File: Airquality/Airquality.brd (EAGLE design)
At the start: 70 x 70 mm, 68 parts, among them IC1 SCD41-D-R2, U1 SGP41-D-R4, U3 BMP581, U4 AP22802AW5-7K-3.3V

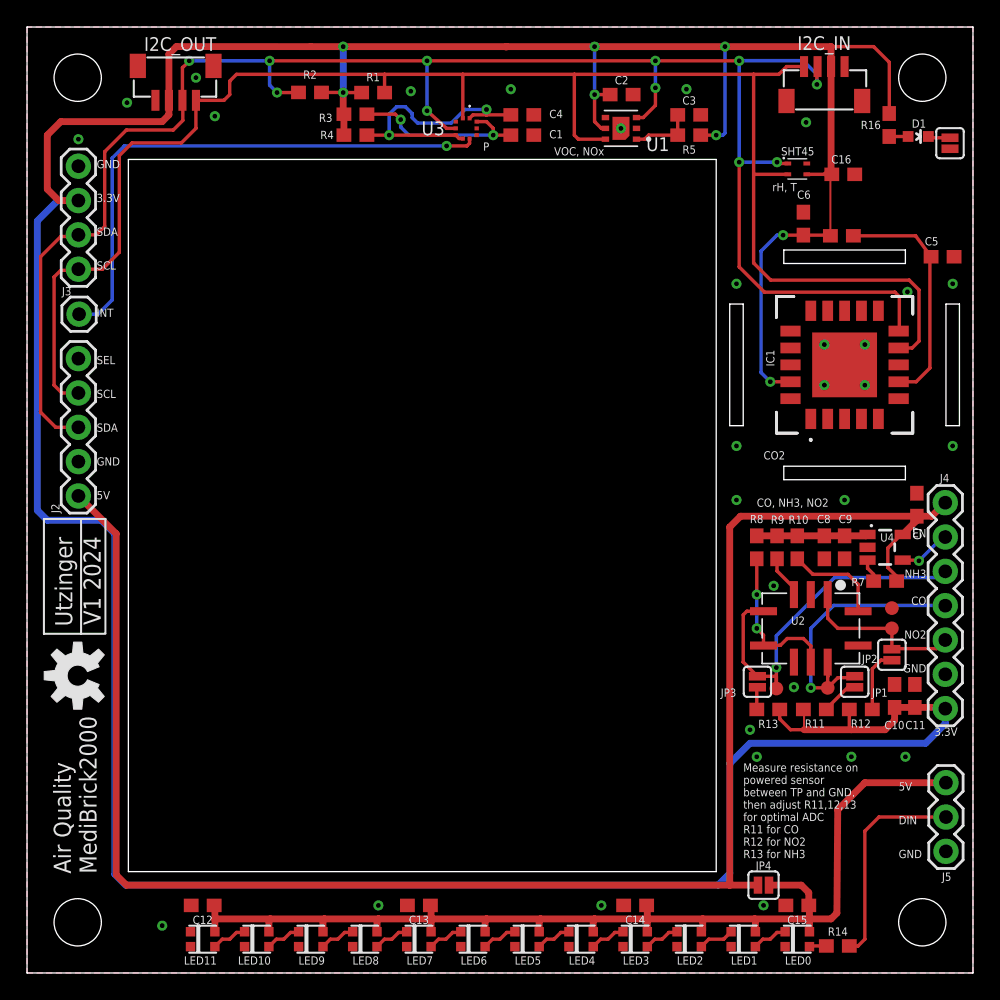
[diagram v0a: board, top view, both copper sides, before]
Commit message: Air Quality at 3.3V with 5V boost for PM sensor
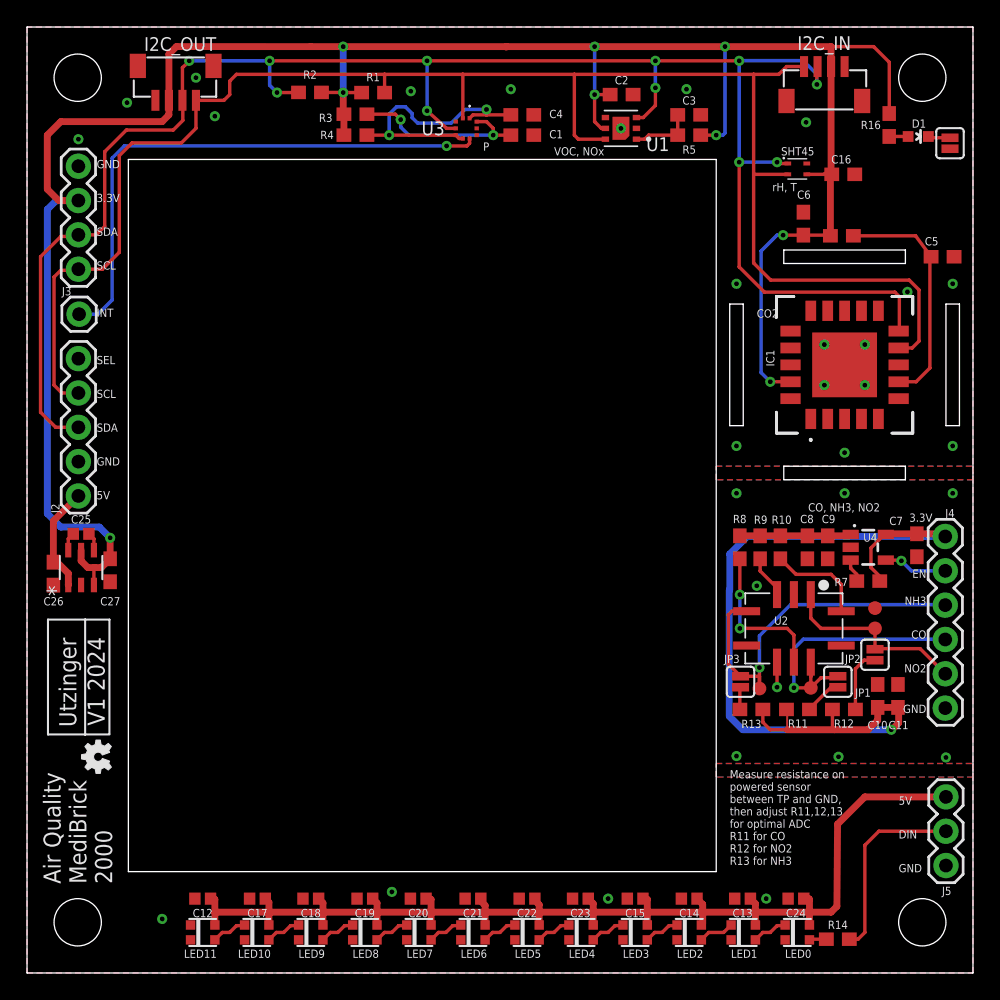
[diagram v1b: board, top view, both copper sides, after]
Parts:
- removed JP4: JUMPER-SMT_2_NO_SILK, SparkFun-Jumpers:SMT-JUMPER_2_NO_SILK
- added C17, C18, C19, C20, C21, C22, C23, C24: 0.1uF, SparkFun-Capacitors:0402
- added C25: 1.0uF, SparkFun-Capacitors:0402
- added C26, C27: 10uF, SparkFun-Capacitors:0603
- added U5: AP3602AKTR-G1, AP3602A:SOT-23-6_DIO
- C12, C13, C14, C15: value 10uF -> 0.1uF; device SparkFun-Capacitors:0603 -> SparkFun-Capacitors:0402
- J4: device SparkFun-Connectors:1X07 -> SparkFun-Connectors:1X06
- R10: value 130 -> 61
- R3: value 10 -> 0
- R4: value 10 -> 4.7
- R8: value 820 -> 29
- R9: value 27 -> 38
- U$2: device SparkFun-Aesthetics:OSHW-LOGO-M -> SparkFun-Aesthetics:OSHW-LOGO-MINI
- moved C13 24.0 mm to (53.0, 5.50)
- moved C15 12.0 mm to (45.0, 5.50)
- moved U$2 6.18 mm to (5.25, 16.0)
- moved C14 4.03 mm to (49.0, 5.50)
- moved C7 3.00 mm to (65.8, 31.6), turned to 270 degrees
- moved J4 2.50 mm to (68.0, 32.3)
- moved C10 1.25 mm to (63.0, 20.5)
- moved C11 1.25 mm to (64.5, 20.5)
- moved C8 1.25 mm to (57.8, 31.5)
- moved C9 1.25 mm to (59.2, 31.5)
- moved CO 1.25 mm to (58.0, 21.1)
- moved GND 1.25 mm to (62.8, 27.0)
- moved JP1 1.25 mm to (60.0, 21.6)
- moved JP2 1.25 mm to (62.8, 23.6)
- moved JP3 1.25 mm to (52.8, 21.6)
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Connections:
- removed net 5V: C12.1, C13.1, C14.1, C15.1, C7.1, J2.1, J4.1, J5.3, JP4.1, JP4.2, LED0.4, LED1.4, LED10.4, LED11.4, LED2.4, LED3.4, LED4.4, LED5.4, LED6.4, LED7.4, LED8.4, LED9.4, R7.1, U4.5
- new net N$15: C25.1, U5.6
- new net N$30: C25.2, U5.4
- new net N$31: C12.1, C13.1, C14.1, C15.1, C17.1, C18.1, C19.1, C20.1, C21.1, C22.1, C23.1, C24.1, J5.3, LED0.4, LED1.4, LED10.4, LED11.4, LED2.4, LED3.4, LED4.4, LED5.4, LED6.4, LED7.4, LED8.4, LED9.4
- new net VOUT: C26.1, J2.1, U5.1
- net 3.3V: now also C27.1, C7.1, J4.1, R7.1, U4.5, U5.3, U5.5; no longer J4.7
- net GND: now also C17.2, C18.2, C19.2, C20.2, C21.2, C22.2, C23.2, C24.2, C26.2, C27.2, U2.E, U5.2
- net N$13: no longer U2.E
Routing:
- net 5V: track 209.7 -> 0.00 mm
- net N$31: track 0.00 -> 87.9 mm
- net 3.3V: track 285.6 -> 242.3 mm, vias 8 -> 10
- net VOUT: track 0.00 -> 7.98 mm
- net GND: track 0.00 -> 1.85 mm, vias 30 -> 31
- net NO2: track 12.6 -> 14.3 mm
- net N$22: track 15.8 -> 14.2 mm
- net N$30: track 0.00 -> 1.36 mm
- net N$15: track 0.00 -> 1.36 mm
- net N$9: track 4.10 -> 4.93 mm
- net CO: track 20.6 -> 19.9 mm
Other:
- board text added: "Air Quality MediBrick 2000"
- board text removed: "Air Quality MediBrick2000"

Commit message: BOM
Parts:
- added FLG: TEST-POINT3X4, SparkFun-Connectors:PAD.03X.04
- added R15: 10k, SparkFun-Resistors:0603
- moved GND 3.16 mm to (65.8, 26.0)
- moved R7 1.00 mm to (62.2, 28.0), turned to 90 degrees
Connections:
- removed net N$9: J4.2, U4.4
- new net N$32: J4.2, R15.2, U4.4
- net 3.3V: now also R15.1
- net N$3: now also FLG.P$1
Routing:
- net N$32: track 0.00 -> 6.72 mm, vias 0 -> 1
- net N$9: track 4.93 -> 0.00 mm, vias 1 -> 0
- net 3.3V: track 242.3 -> 246.2 mm
- net N$3: track 1.74 -> 2.59 mm
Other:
- outline, holes or cut-outs redrawn

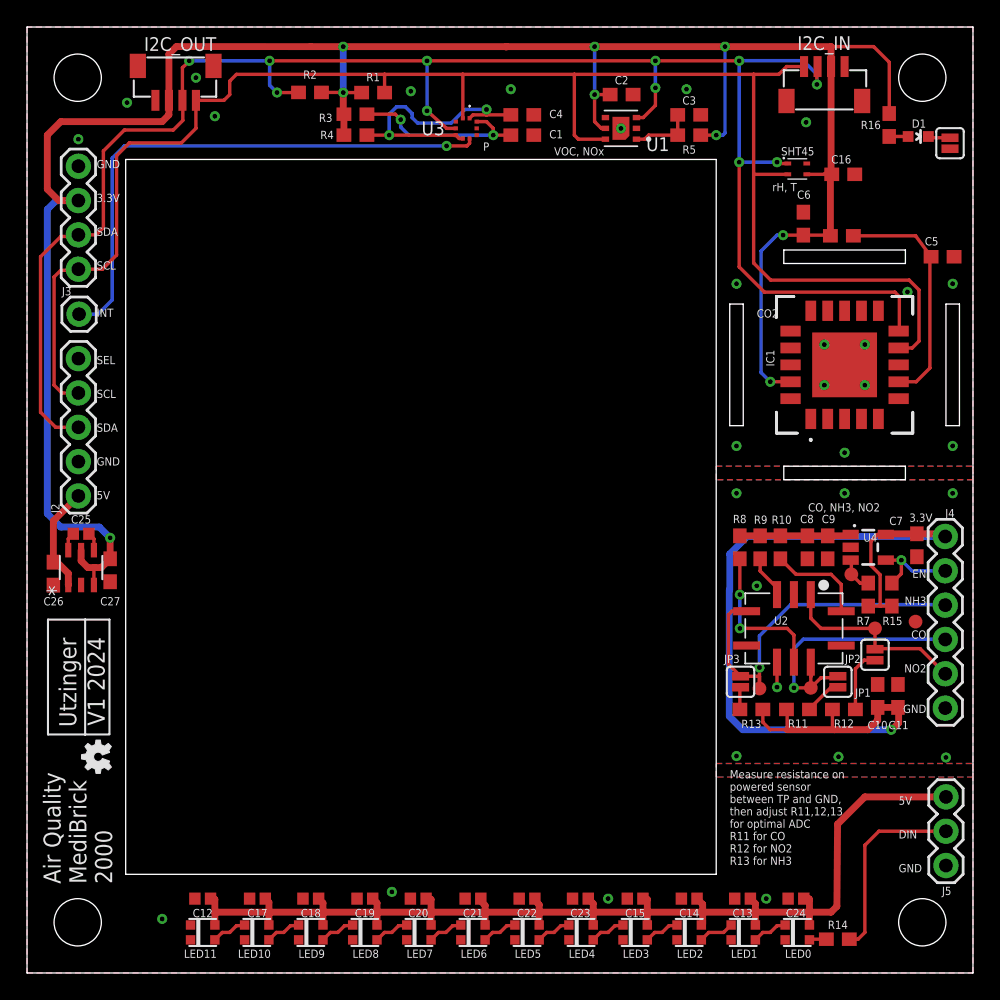
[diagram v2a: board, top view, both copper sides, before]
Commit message: IMU board
Completed IMU board design
Updated designs with ground via close to any other via.
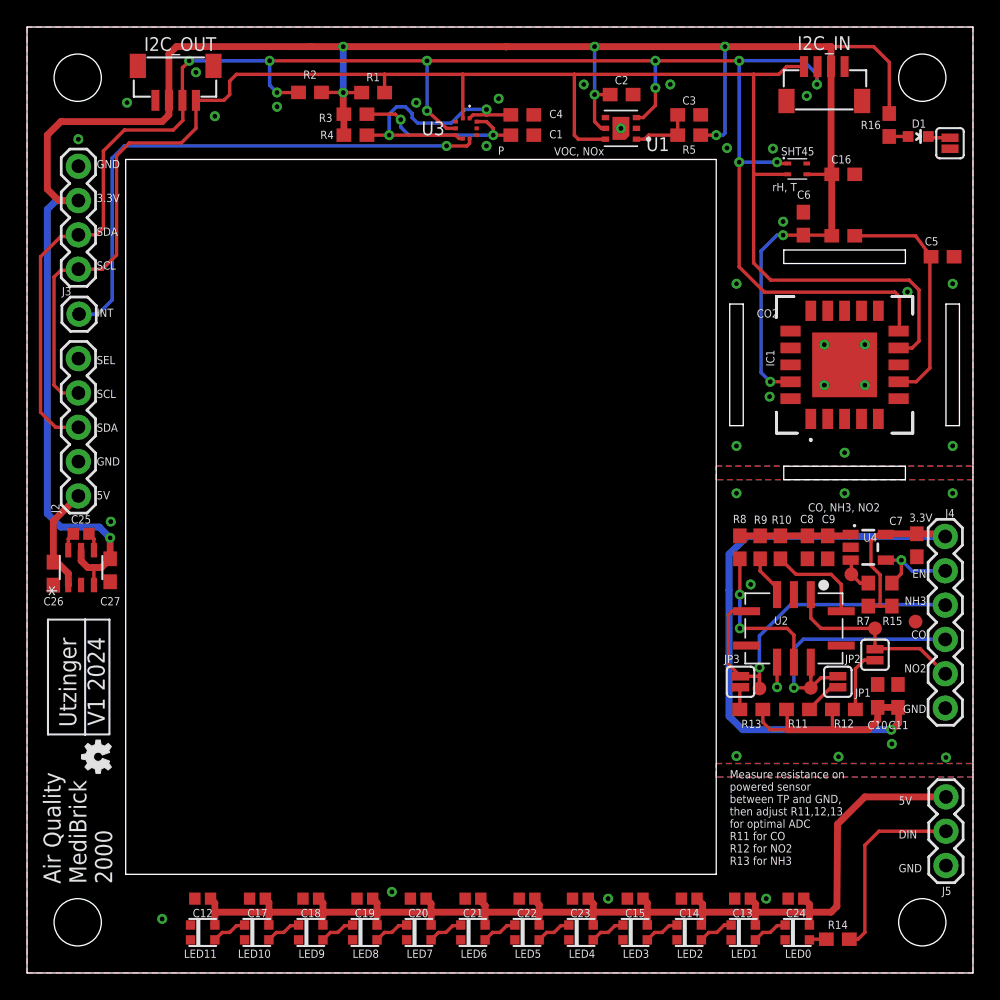
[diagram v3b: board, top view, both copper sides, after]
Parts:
- moved R6 0.10 mm to (60.4, 54.5)
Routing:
- net GND: vias 31 -> 40

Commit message: Production Updates
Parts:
- U5: device AP3602A:SOT-23-6_DIO -> AP3602AKTR-G1:SOT95P280X125-6N
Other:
- board text added: "3.3-5V"
- board text removed: "5V"

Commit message: Merging Production Status to Github, Obtaining senior design files
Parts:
- moved C26 0.51 mm to (1.50, 29.8)
- moved C25 0.20 mm to (4.00, 32.7)
- moved C27 0.10 mm to (6.25, 29.8)
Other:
- board text added: "3.3- 5V"

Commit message: Major Update
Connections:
- net 3.3V: no longer R15.1
- net GND: now also R15.1
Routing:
- net 3.3V: track 246.3 -> 245.4 mm
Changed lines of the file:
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@@
 <via x="64" y="16.95" extent="1-16" drill="0.35"/>
 <via x="6.25" y="33.65" extent="1-16" drill="0.35"/>
+<contactref element="R15" pad="1"/>
 <wire x1="60.5" y1="35.5" x2="60.5" y2="38.5" width="0" layer="19" extent="1-1"/>
 </signal>
@@
 <wire x1="6.25" y1="30.65" x2="6.25" y2="32.2" width="0.508" layer="1"/>
 <wire x1="6.25" y1="32.2" x2="5.35" y2="33" width="0.508" layer="16"/>
-<contactref element="R15" pad="1"/>
 <wire x1="62.25" y1="27.15" x2="63.1294" y2="27.15" width="0.254" layer="1"/>
-<wire x1="63.1294" y1="27.15" x2="64" y2="27.15" width="0.254" layer="1"/>
 <wire x1="63.1294" y1="27.15" x2="63.1294" y2="29.4706" width="0.254" layer="1"/>
 <wire x1="63.1294" y1="29.4706" x2="62.45" y2="30.15" width="0.254" layer="1"/>
